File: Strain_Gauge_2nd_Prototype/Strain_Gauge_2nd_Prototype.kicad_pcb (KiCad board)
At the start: 2 copper layers, 87 parts, among them J1 TC2030, J10 2601-1104, J11 Molex_104031-0811, J3 Conn_01x04, J4 Conn_01x04, J5 Conn_01x04, J6 Conn_01x04, J7 Conn_01x04, J8 Conn_01x04, Q1 PMV100EPA, SW1 SW_Push, U1 ADS131M08xPBS, U2 STM32F446RETx, U4 MCP2562-E-SN, U5 LMR33610ADDAR, Y1 7XL-8.192MBD-T

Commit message: The netlist has been updated for the schematic for review
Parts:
- J3, J4, J5, J6, J7, J8: footprint Connector_Wire:SolderWire-0.25sqmm_1x04_P4.5mm_D0.65mm_OD2mm_Relief2x -> Connector_Wire:SolderWire-0.25sqmm_1x04_P4.5mm_D0.65mm_OD2mm

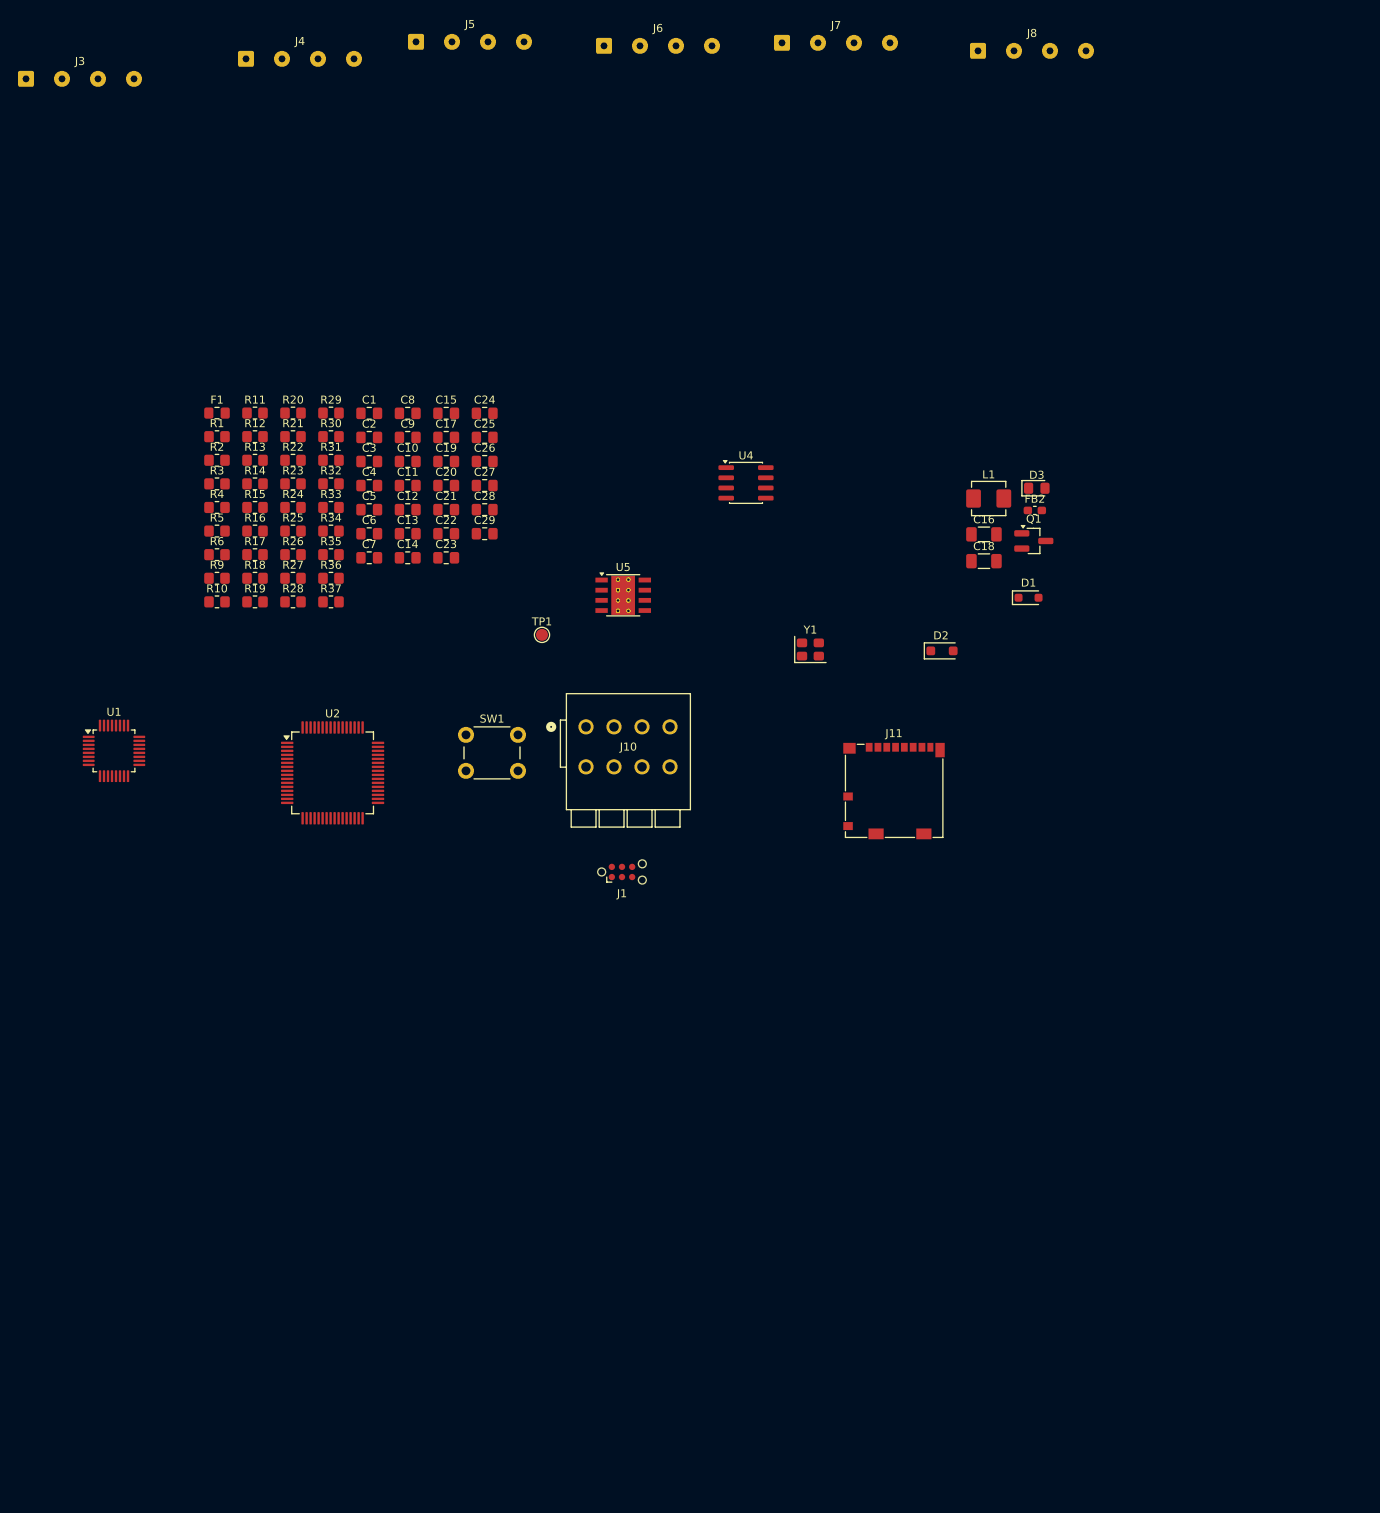
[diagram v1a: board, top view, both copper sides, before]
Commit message: PCB components are laid out, need to position, then route.
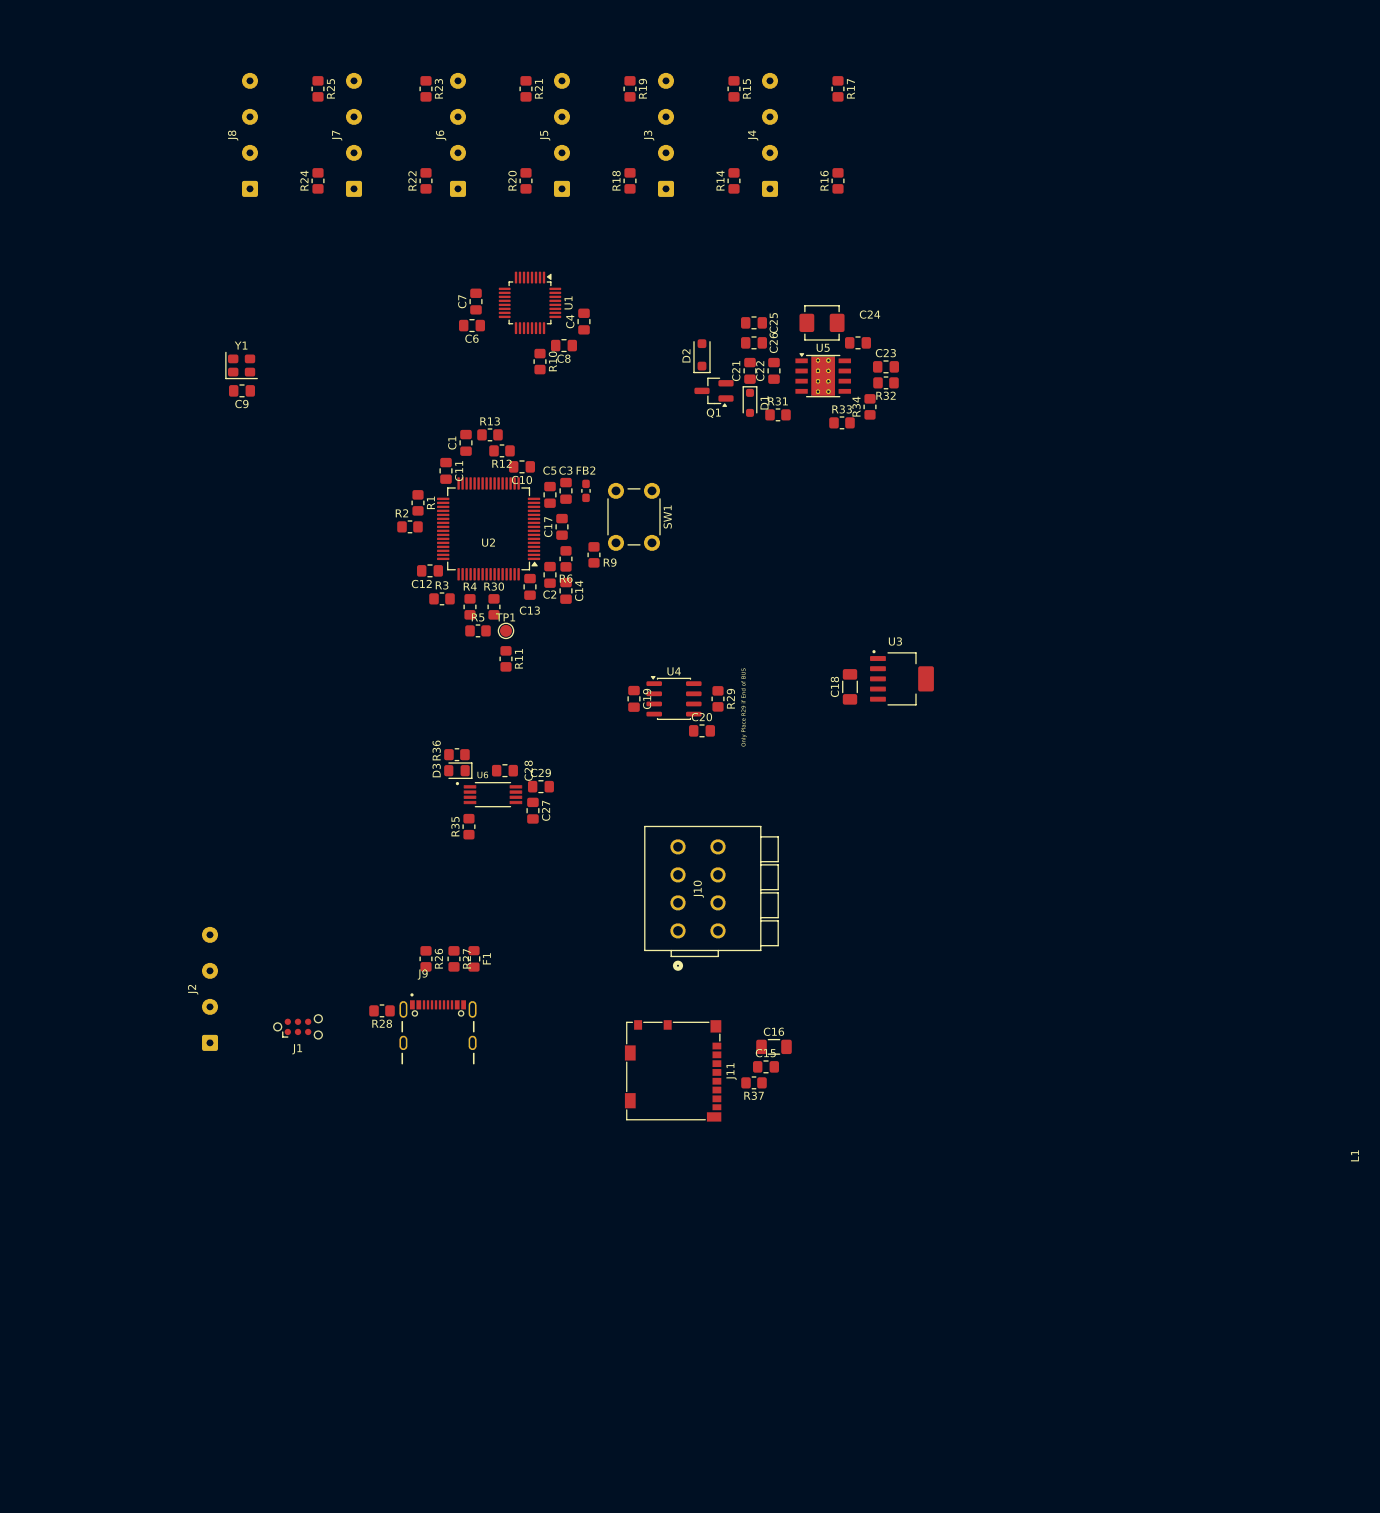
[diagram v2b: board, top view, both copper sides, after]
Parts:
- added J2: Conn_01x04, Connector_Wire:SolderWire-0.25sqmm_1x04_P4.5mm_D0.65mm_OD2mm, F.Cu at (82.5, 162.0)
- added J9: USB4105-GF-A-060, Gauge Footprints:GCT_USB4105-GF-A-060, F.Cu at (111.0, 162.0)
- added U3: TPS73733DCQ, Gauge Footprints:SOT127P706X180-6N, F.Cu at (169.0, 116.5)
- added U6: TPS2113APWR, Gauge Footprints:SOP65P640X120-8N, F.Cu at (117.9, 131.0)
- moved R17 93.3 mm to (161.0, 42.8), turned to -90 degrees
- moved J8 92.6 mm to (87.5, 55.2), turned to 90 degrees
- moved C15 91.0 mm to (152.0, 165.0)
- moved R16 85.0 mm to (161.0, 54.2), turned to 90 degrees
- moved J3 81.2 mm to (139.5, 55.2), turned to 90 degrees
- moved D3 80.6 mm to (113.4, 128.0), turned to 180 degrees
- moved R37 80.1 mm to (150.5, 167.0), turned to 180 degrees
- moved R15 79.5 mm to (148.0, 42.8), turned to -90 degrees
- moved Y1 79.5 mm to (86.5, 77.3)
- moved R19 79.4 mm to (135.0, 42.8), turned to -90 degrees
- moved U1 76.4 mm to (122.5, 69.5), turned to -90 degrees
- moved F1 75.4 mm to (115.5, 151.5), turned to -90 degrees
- moved R14 70.8 mm to (148.0, 54.2), turned to 90 degrees
- moved R32 70.5 mm to (167.0, 79.5), turned to 180 degrees
- moved C16 69.2 mm to (153.0, 162.5)
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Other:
- board text added: "Only Place R29 if End of BUS"

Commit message: This is the update with STM32CUBEMX and IDE, to check syntax
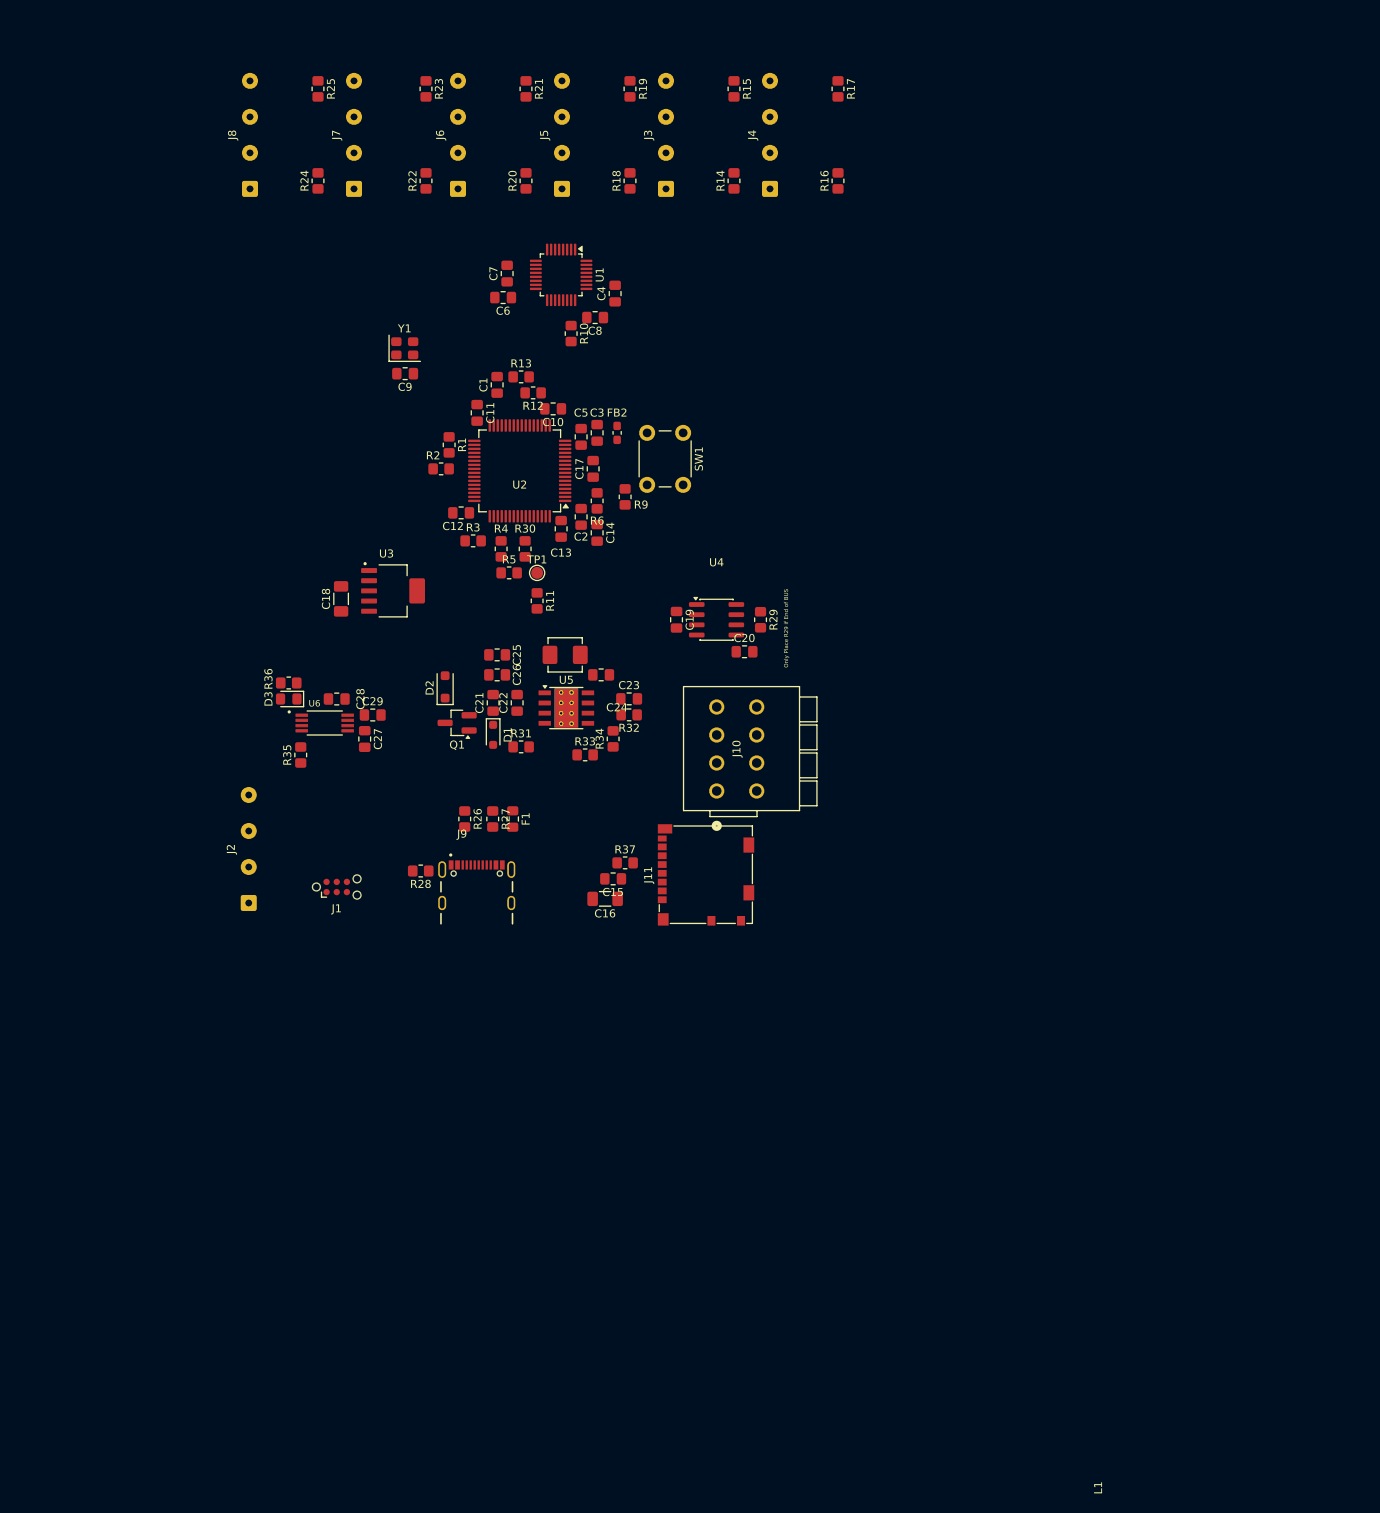
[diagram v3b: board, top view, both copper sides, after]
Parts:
- moved C18 64.6 mm to (98.9, 106.5)
- moved U3 64.6 mm to (105.4, 105.5)
- moved C23 52.5 mm to (134.9, 119.0)
- moved C24 52.5 mm to (131.4, 116.0)
- moved R32 52.5 mm to (134.9, 121.0)
- moved R33 52.5 mm to (129.4, 126.0)
- moved R34 52.5 mm to (132.9, 124.0)
- moved U5 52.5 mm to (127.0, 120.2)
- moved C21 52.5 mm to (117.9, 119.5)
- moved C22 52.5 mm to (120.9, 119.5)
- moved C25 52.5 mm to (118.4, 113.5)
- moved C26 52.5 mm to (118.4, 116.0)
- moved D1 52.5 mm to (117.9, 123.5)
- moved D2 52.5 mm to (111.9, 117.5)
- moved L1 52.5 mm to (126.9, 113.5)
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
